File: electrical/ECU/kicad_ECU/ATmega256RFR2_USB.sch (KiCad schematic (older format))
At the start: 29 parts

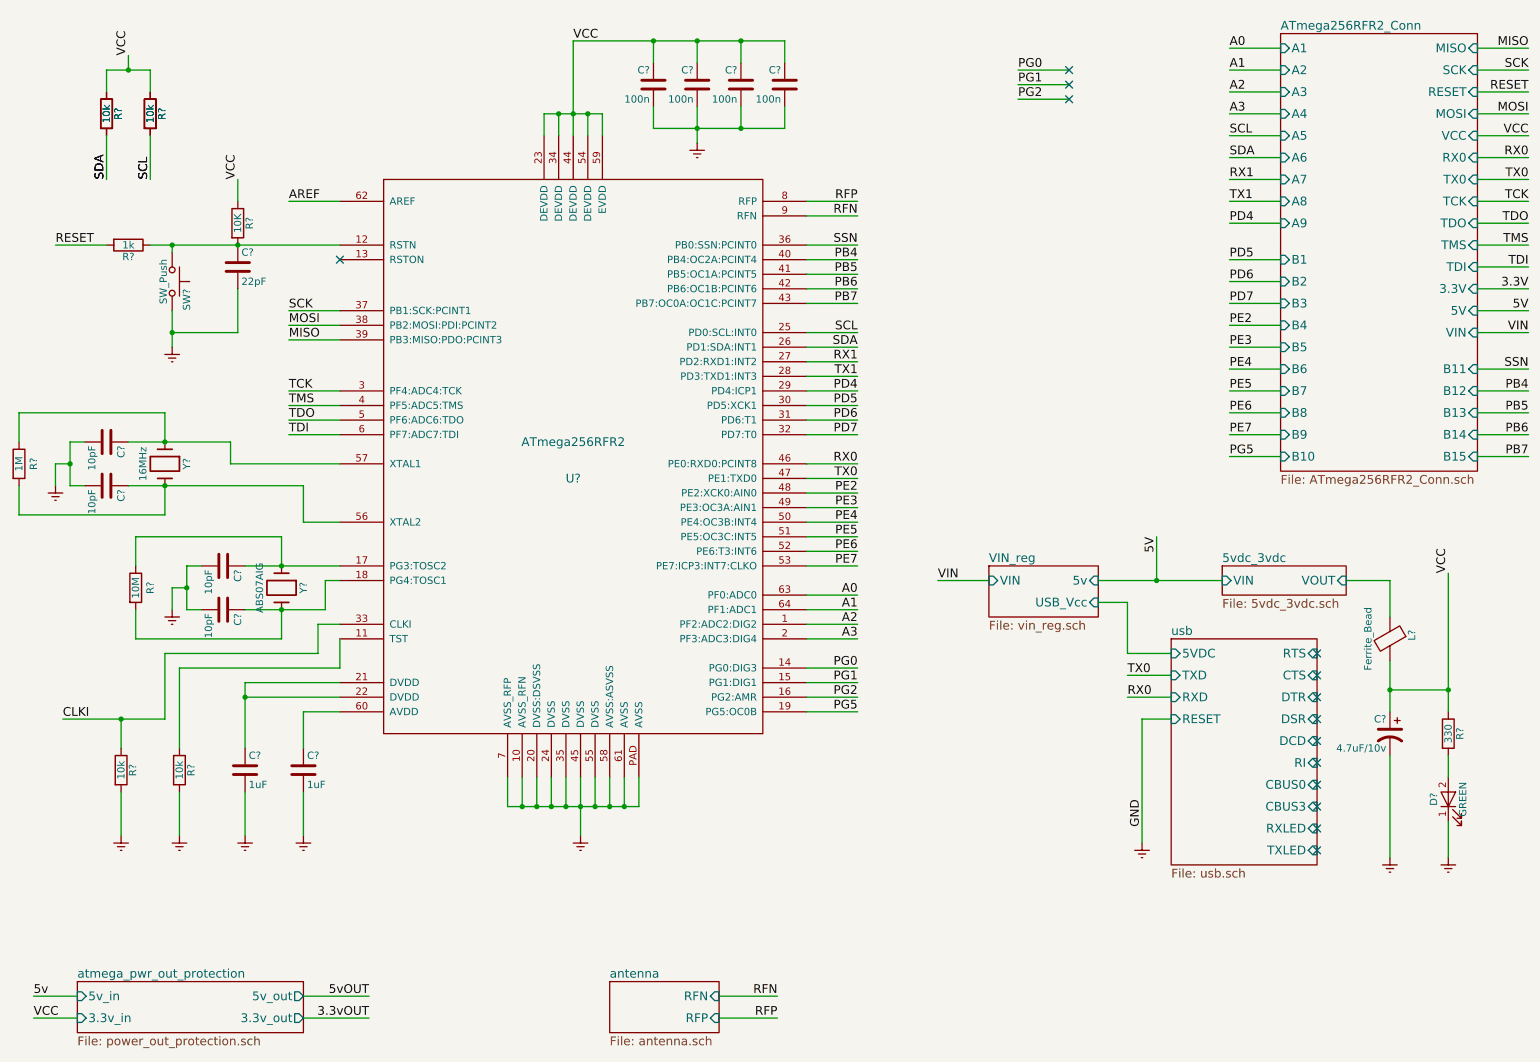
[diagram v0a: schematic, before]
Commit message: fixed some naming errors and initial round of double checking
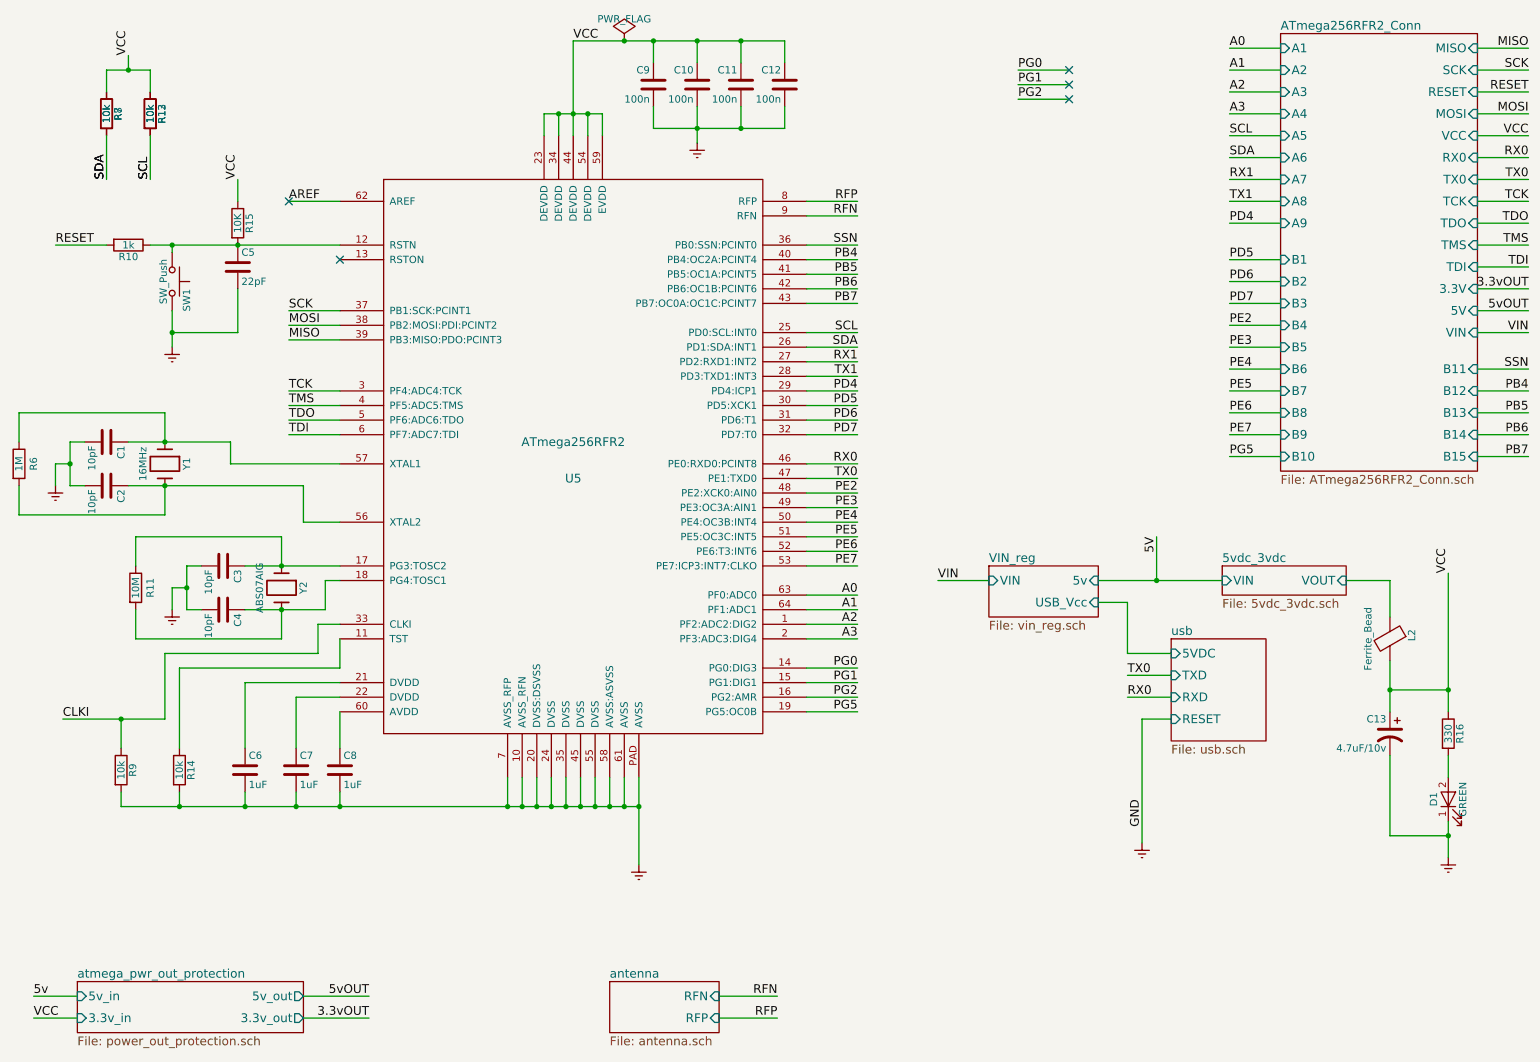
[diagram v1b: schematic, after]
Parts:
- added C7: 1uF, symbol C
- gave numbers to parts that had none: 29
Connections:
- net Earth: now also C7.2
- net at C6.1, U5.21 (DVDD): no longer U5.22 (DVDD)
- new net: C7.1, U5.22 (DVDD)
- no-connect marks 14 -> 5
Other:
- moved on the sheet: C8
